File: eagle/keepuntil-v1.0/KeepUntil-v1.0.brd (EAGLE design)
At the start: 100 x 80 mm, 25 parts, among them IC1 REG1117, Q1 CSTCR6M00G53Z, T1 BC846, U1 ATMEGA328P-AU, X1 MINI-USB-32005-201

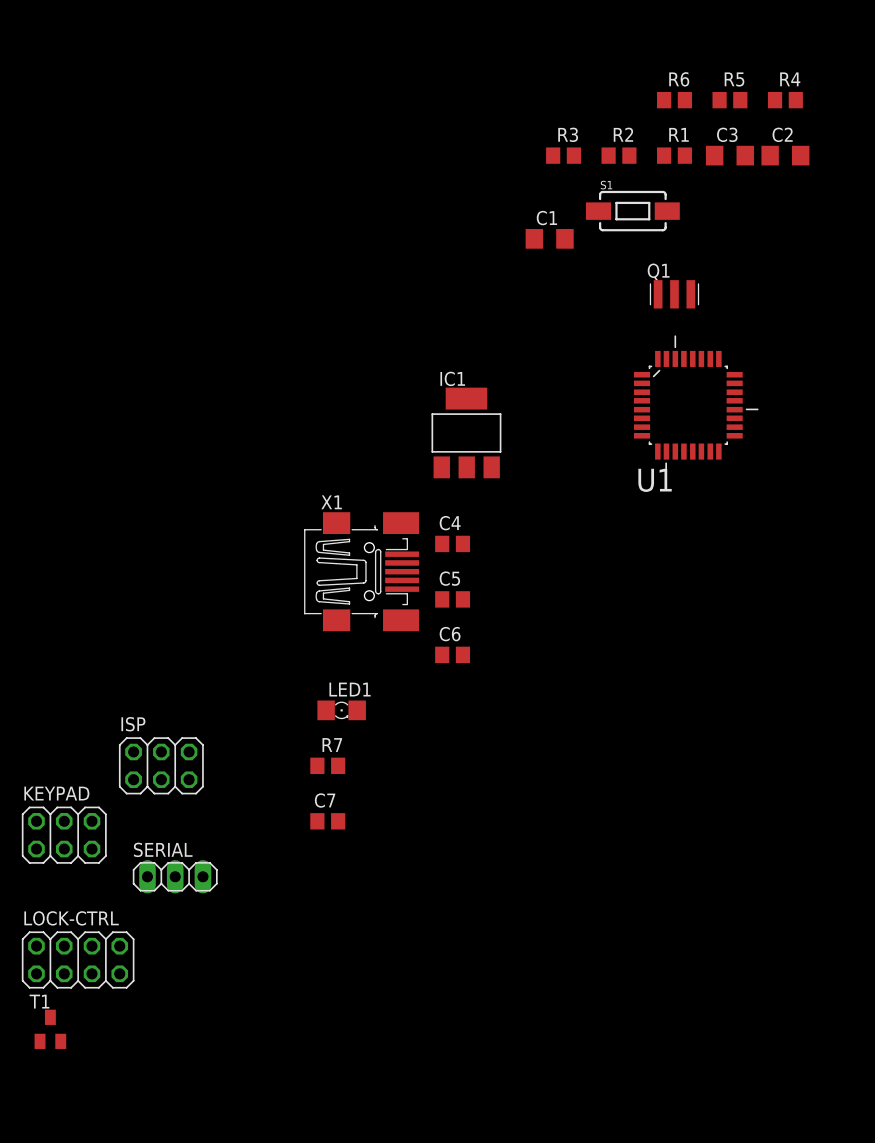
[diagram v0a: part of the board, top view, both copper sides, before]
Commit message: remove unnecessary eagle file
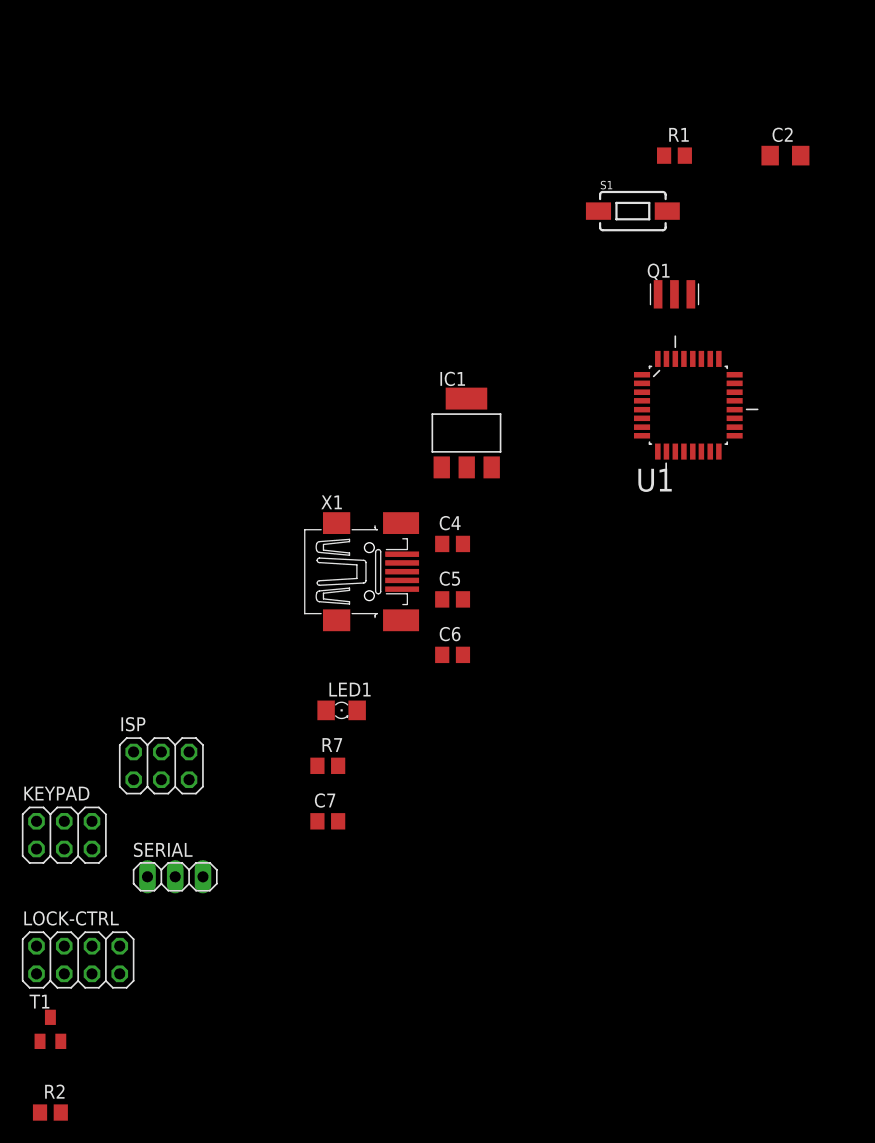
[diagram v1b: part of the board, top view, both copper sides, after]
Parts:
- removed C1, C3: (no value), resistor:C1206
- removed R3, R4, R5, R6: (no value), resistor:R0805
- moved R2 101.9 mm to (-82.5, -55.9)
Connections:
- removed net N$12: LOCK-CTRL.2
- removed net N$13: LOCK-CTRL.4
- removed net N$6: C1.2, C3.1
- new net N$3: R2.1, T1.1
- new net SOLENOID-SIG: R2.2, U1.32
- net SOLENOID: now also LOCK-CTRL.2, T1.3; no longer U1.32
- net VCC: now also LOCK-CTRL.4
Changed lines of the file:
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@@
 </autorouter>
 <elements>
-<element name="C1" library="resistor" package="C1206" value="" x="-36.83" y="24.13"/>
 <element name="C2" library="resistor" package="C1206" value="" x="-15.24" y="31.75"/>
-<element name="C3" library="resistor" package="C1206" value="" x="-20.32" y="31.75"/>
 <element name="Q1" library="murata-filter" package="CSTCR6M" value="CSTCR6M00G53Z" x="-25.4" y="19.05">
 <attribute name="MF" value="" x="-25.4" y="19.05" size="1.778" layer="27" display="off"/>
@@
 </element>
 <element name="R1" library="resistor" package="R0805" value="" x="-25.4" y="31.75"/>
-<element name="R2" library="resistor" package="R0805" value="" x="-30.48" y="31.75"/>
-<element name="R3" library="resistor" package="R0805" value="" x="-35.56" y="31.75"/>
-<element name="R4" library="resistor" package="R0805" value="" x="-15.24" y="36.83"/>
-<element name="R5" library="resistor" package="R0805" value="" x="-20.32" y="36.83"/>
-<element name="R6" library="resistor" package="R0805" value="" x="-25.4" y="36.83"/>
 <element name="S1" library="SparkFun-Electromechanical" package="TACTILE-SWITCH-1101NE" value="SWITCH-MOMENTARY-2SMD-1101NE" x="-29.21" y="26.67">
 <attribute name="PROD_ID" value="SWCH-00815" x="-29.21" y="26.67" size="1.778" layer="27" display="off"/>
@@
 <element name="LOCK-CTRL" library="pinhead" package="2X04" value="" x="-80.01" y="-41.91"/>
 <element name="T1" library="transistor" package="SOT23" value="BC846" x="-82.55" y="-48.26"/>
+<element name="R2" library="resistor" package="R0805" value="" x="-82.55" y="-55.88"/>
 </elements>
 <signals>
@@
 <contactref element="U1" pad="4"/>
 <contactref element="R1" pad="2"/>
-<contactref element="R7" pad="2"/>
 <contactref element="C7" pad="1"/>
 <contactref element="ISP" pad="2"/>
 <contactref element="LOCK-CTRL" pad="3"/>
-<wire x1="-74.93" y1="-22.86" x2="-81.28" y2="-43.18" width="0" layer="19" extent="1-1"/>
+<contactref element="R7" pad="2"/>
+<contactref element="LOCK-CTRL" pad="4"/>
+<wire x1="-81.28" y1="-40.64" x2="-81.28" y2="-43.18" width="0" layer="19" extent="1-1"/>
+<wire x1="-74.93" y1="-22.86" x2="-81.28" y2="-40.64" width="0" layer="19" extent="1-1"/>
 <wire x1="-58.1" y1="-29.21" x2="-74.93" y2="-22.86" width="0" layer="19" extent="1-1"/>
 <wire x1="-56.2" y1="-24.13" x2="-58.1" y2="-29.21" width="0" layer="19" extent="1-1"/>
@@
 <wire x1="-13.84" y1="31.75" x2="-26.06" y2="26.67" width="0" layer="19" extent="1-1"/>
 </signal>
-<signal name="N$6">
-<contactref element="C1" pad="2"/>
-<contactref element="C3" pad="1"/>
-<wire x1="-21.72" y1="31.75" x2="-35.43" y2="24.13" width="0" layer="19" extent="1-1"/>
-</signal>
 <signal name="N$7">
 <contactref element="LED1" pad="A"/>
@@
 </signal>
 <signal name="ROW3">
+<contactref element="KEYPAD" pad="5"/>
 <contactref element="U1" pad="11"/>
-<contactref element="KEYPAD" pad="5"/>
 <wire x1="-25.3238" y1="4.6482" x2="-78.74" y2="-31.75" width="0" layer="19" extent="1-1"/>
 </signal>
@@
 <wire x1="-28.3718" y1="11.684" x2="-83.82" y2="-43.18" width="0" layer="19" extent="1-1"/>
 </signal>
-<signal name="SOLENOID">
+<signal name="SOLENOID-SIG">
 <contactref element="U1" pad="32"/>
+<contactref element="R2" pad="2"/>
+<wire x1="-26.924" y1="13.1318" x2="-81.6" y2="-55.88" width="0" layer="19" extent="1-1"/>
 </signal>
 <signal name="LEDGRN">
@@
 <wire x1="-19.8882" y1="11.684" x2="-76.2" y2="-40.64" width="0" layer="19" extent="1-1"/>
 </signal>
-<signal name="N$12">
-<contactref element="LOCK-CTRL" pad="2"/>
-</signal>
-<signal name="N$13">
-<contactref element="LOCK-CTRL" pad="4"/>
-</signal>
 <signal name="N$9">
 <contactref element="LOCK-CTRL" pad="5"/>
 </signal>
+<signal name="N$3">
+<contactref element="R2" pad="1"/>
+<contactref element="T1" pad="1"/>
+<wire x1="-83.5" y1="-49.36" x2="-83.5" y2="-55.88" width="0" layer="19" extent="1-1"/>
+</signal>
+<signal name="SOLENOID">
+<contactref element="LOCK-CTRL" pad="2"/>
+<contactref element="T1" pad="3"/>
+<wire x1="-83.82" y1="-40.64" x2="-82.55" y2="-47.16" width="0" layer="19" extent="1-1"/>
+</signal>
 </signals>

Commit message: update schematic
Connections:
- net 3.3V: now also T1.2
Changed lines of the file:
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@@
 <contactref element="ISP" pad="6"/>
 <contactref element="SERIAL" pad="3"/>
+<contactref element="T1" pad="2"/>
+<wire x1="-68.58" y1="-34.29" x2="-81.6" y2="-49.36" width="0" layer="19" extent="1-1"/>
 <wire x1="-69.85" y1="-22.86" x2="-68.58" y2="-34.29" width="0" layer="19" extent="1-1"/>
 <wire x1="-56.2" y1="-29.21" x2="-68.58" y2="-34.29" width="0" layer="19" extent="1-1"/>

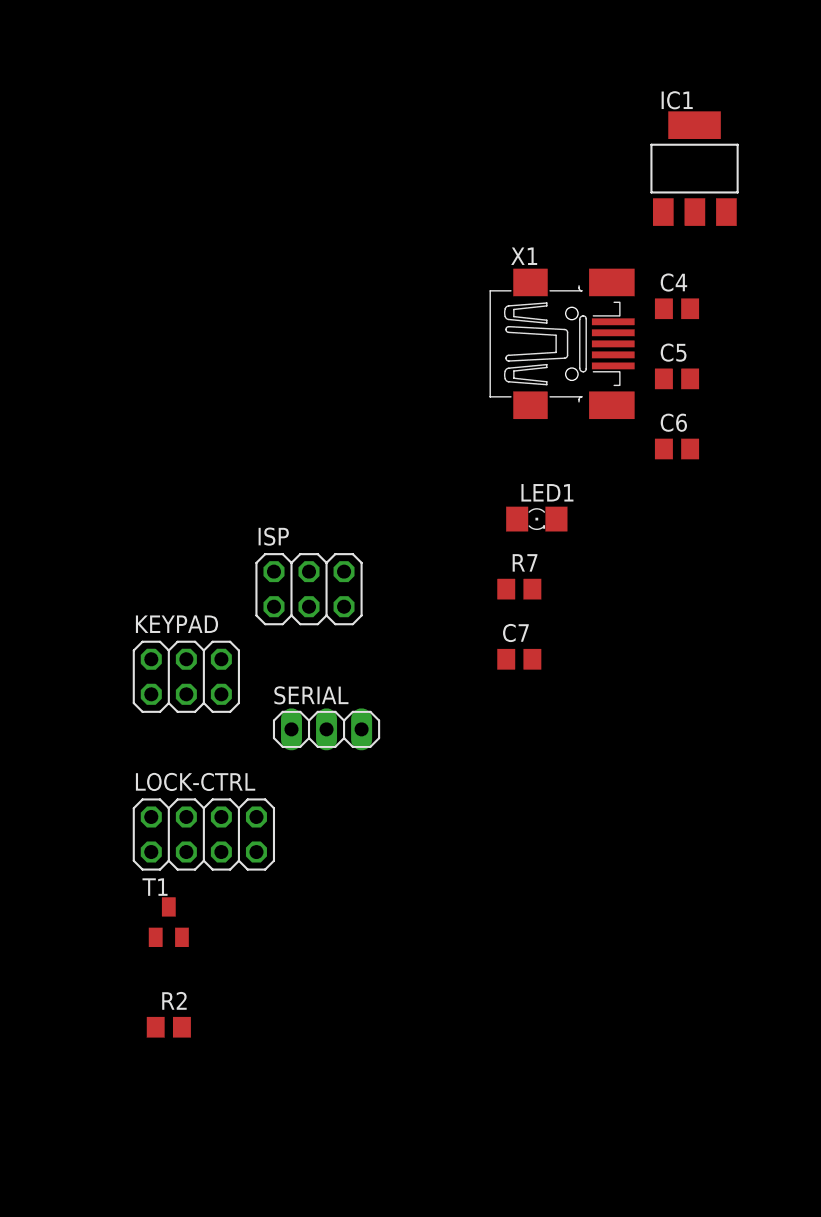
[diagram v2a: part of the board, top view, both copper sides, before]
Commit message: update schematic
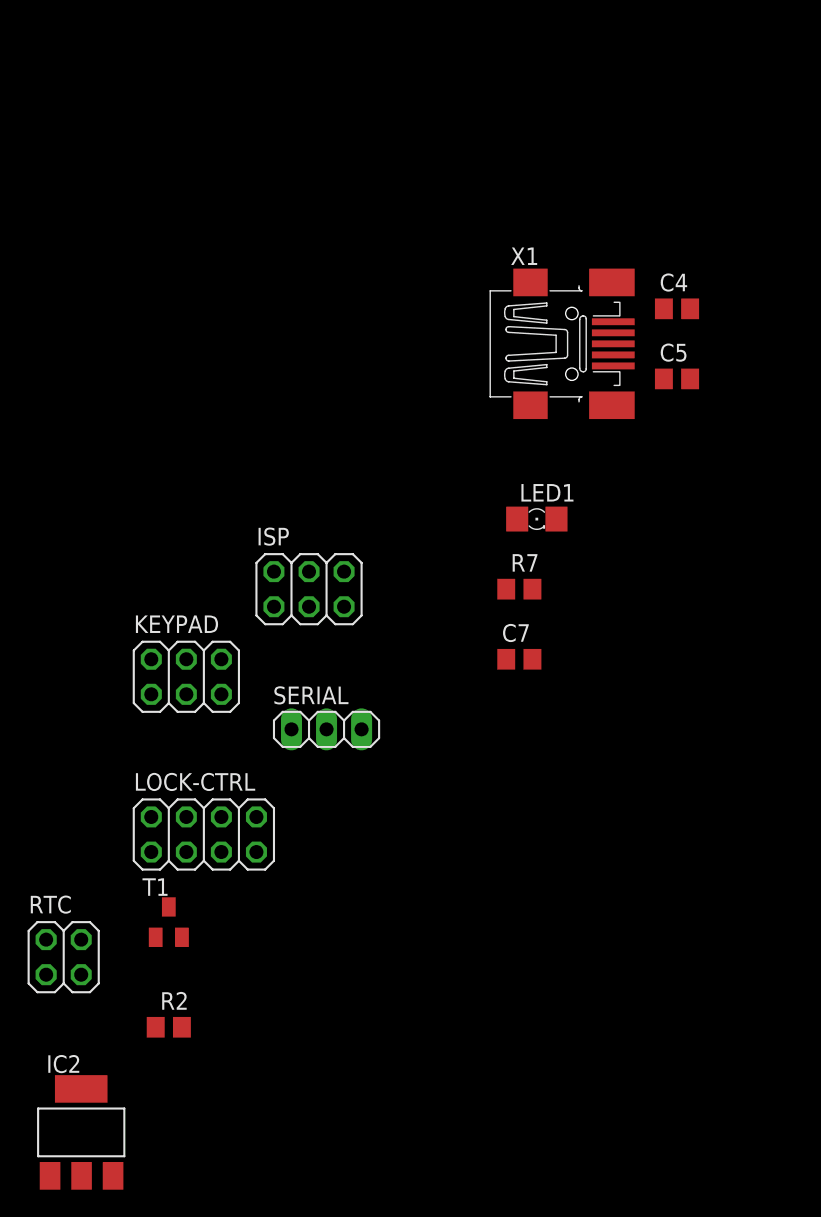
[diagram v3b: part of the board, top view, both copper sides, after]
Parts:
- removed C6: (no value), resistor:C0805
- removed IC1: REG1117, burr-brown:SOT223
- added IC2: REG1117, burr-brown:SOT223
- added RTC: (no value), pinhead:2X02
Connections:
- net LEDGRN renamed LED-GRN
- net LEDRED renamed LED-RED
- removed net 3.3V: C2.2, C4.2, C5.2, C7.2, IC1.1, ISP.6, LED1.C, S1.2, SERIAL.3, T1.2, X1.5
- removed net N$5: C4.1, IC1.3, X1.1
- removed net N$9: LOCK-CTRL.5
- removed net SCL: U1.28
- new net GND: C2.2, C4.2, C5.2, C7.2, IC2.1, ISP.6, LED1.C, LOCK-CTRL.5, RTC.4, S1.2, SERIAL.3, T1.2, U1.21, U1.3, U1.5, X1.5
- new net RTC-SCL: RTC.3, U1.28
- new net RTC-SDA: RTC.1, U1.27
- net N$4: now also C4.1, IC2.3, X1.1; no longer U1.21, U1.3, U1.5
- net VCC: now also IC2.2, RTC.2; no longer IC1.2

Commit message: schematic cleanup
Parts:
- removed C7: (no value), resistor:C0805
- removed SERIAL: (no value), pinhead:1X03
- added JP1: (no value), adafruit:1X03
- C2: value (none) -> 10uf
- C4, C5: value (none) -> 0.1uF
- R1: value (none) -> 1K
- R2: value (none) -> 10K
- R7: value (none) -> 330
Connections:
- net GND: now also JP1.3; no longer C7.2, SERIAL.3
- net RX: now also JP1.1; no longer SERIAL.1
- net TX: now also JP1.2; no longer SERIAL.2
- net VCC: no longer C7.1
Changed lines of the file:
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@@
 <setting verticaltext="up"/>
 </settings>
-<grid distance="0.05" unitdist="inch" unit="inch" style="lines" multiple="1" display="no" altdistance="0.025" altunitdist="inch" altunit="inch"/>
+<grid distance="0.5" unitdist="mm" unit="mm" style="lines" multiple="1" display="no" altdistance="0.1" altunitdist="mm" altunit="mm"/>
 <layers>
 <layer number="1" name="Top" color="4" fill="1" visible="yes" active="yes"/>
@@
 <layer number="43" name="vRestrict" color="2" fill="10" visible="yes" active="yes"/>
 <layer number="44" name="Drills" color="7" fill="1" visible="no" active="yes"/>
-<layer number="45" name="Holes" color="7" fill="1" visible="no" active="yes"/>
+<layer number="45" name="Holes" color="7" fill="1" visible="yes" active="yes"/>
 <layer number="46" name="Milling" color="3" fill="1" visible="no" active="yes"/>
 <layer number="47" name="Measures" color="7" fill="1" visible="no" active="yes"/>
@@
 </autorouter>
 <elements>
-<element name="C2" library="resistor" package="C1206" value="" x="-15.24" y="31.75"/>
+<element name="C2" library="resistor" package="C1206" value="10uf" x="-15.24" y="31.75"/>
 <element name="Q1" library="murata-filter" package="CSTCR6M" value="CSTCR6M00G53Z" x="-25.4" y="19.05">
 <attribute name="MF" value="" x="-25.4" y="19.05" size="1.778" layer="27" display="off"/>
@@
 <attribute name="OC_NEWARK" value="25M8759" x="-25.4" y="19.05" size="1.778" layer="27" display="off"/>
 </element>
-<element name="R1" library="resistor" package="R0805" value="" x="-25.4" y="31.75"/>
+<element name="R1" library="resistor" package="R0805" value="1K" x="-25.4" y="31.75"/>
 <element name="S1" library="SparkFun-Electromechanical" package="TACTILE-SWITCH-1101NE" value="SWITCH-MOMENTARY-2SMD-1101NE" x="-29.21" y="26.67">
 <attribute name="PROD_ID" value="SWCH-00815" x="-29.21" y="26.67" size="1.778" layer="27" display="off"/>
@@
 <attribute name="OC_NEWARK" value="14R4631" x="-24.13" y="8.89" size="1.778" layer="27" display="off"/>
 </element>
-<element name="C4" library="resistor" package="C0805" value="" x="-45.72" y="-3.81"/>
-<element name="C5" library="resistor" package="C0805" value="" x="-45.72" y="-8.89"/>
+<element name="C4" library="resistor" package="C0805" value="0.1uF" x="-45.72" y="-3.81"/>
+<element name="C5" library="resistor" package="C0805" value="0.1uF" x="-45.72" y="-8.89"/>
 <element name="X1" library="con-cypressindustries" package="32005-201" value="MINI-USB-32005-201" x="-53.34" y="-6.35">
 <attribute name="OC_FARNELL" value="unknown" x="-53.34" y="-6.35" size="1.778" layer="27" display="off"/>
@@
 </element>
 <element name="LED1" library="led" package="1206" value="" x="-55.88" y="-19.05"/>
-<element name="R7" library="resistor" package="R0805" value="" x="-57.15" y="-24.13"/>
-<element name="C7" library="resistor" package="C0805" value="" x="-57.15" y="-29.21"/>
+<element name="R7" library="resistor" package="R0805" value="330" x="-57.15" y="-24.13"/>
 <element name="ISP" library="pinhead" package="2X03" value="" x="-72.39" y="-24.13"/>
-<element name="SERIAL" library="pinhead" package="1X03" value="" x="-71.12" y="-34.29"/>
 <element name="KEYPAD" library="pinhead" package="2X03" value="" x="-81.28" y="-30.48"/>
 <element name="LOCK-CTRL" library="pinhead" package="2X04" value="" x="-80.01" y="-41.91"/>
 <element name="T1" library="transistor" package="SOT23" value="BC846" x="-82.55" y="-48.26"/>
-<element name="R2" library="resistor" package="R0805" value="" x="-82.55" y="-55.88"/>
+<element name="R2" library="resistor" package="R0805" value="10K" x="-82.55" y="-55.88"/>
 <element name="RTC" library="pinhead" package="2X02" value="" x="-90.17" y="-50.8"/>
 <element name="IC2" library="burr-brown" package="SOT223" value="REG1117" x="-88.9" y="-63.5">
@@
 <attribute name="MF" value="" x="-97.79" y="-49.53" size="1.778" layer="27" display="off"/>
 </element>
+<element name="JP1" library="adafruit" package="1X03" value="" x="-87.63" y="-73.66"/>
 </elements>
 <signals>
@@
 <signal name="TX">
 <contactref element="U1" pad="31"/>
-<contactref element="SERIAL" pad="2"/>
-<wire x1="-26.1366" y1="13.1318" x2="-71.12" y2="-34.29" width="0" layer="19" extent="1-1"/>
+<contactref element="JP1" pad="2"/>
+<wire x1="-26.1366" y1="13.1318" x2="-87.63" y2="-73.66" width="0" layer="19" extent="1-1"/>
 </signal>
 <signal name="RX">
 <contactref element="U1" pad="30"/>
-<contactref element="SERIAL" pad="1"/>
-<wire x1="-25.3238" y1="13.1318" x2="-73.66" y2="-34.29" width="0" layer="19" extent="1-1"/>
+<contactref element="JP1" pad="1"/>
+<wire x1="-25.3238" y1="13.1318" x2="-90.17" y2="-73.66" width="0" layer="19" extent="1-1"/>
 </signal>
 <signal name="ROW1">
@@
 <contactref element="IC2" pad="2"/>
 <contactref element="C2" pad="1"/>
-<contactref element="C7" pad="1"/>
 <contactref element="R7" pad="2"/>
 <wire x1="-91.44" y1="-49.53" x2="-88.8746" y2="-66.6496" width="0" layer="19" extent="1-1"/>
@@
 <wire x1="-81.28" y1="-40.64" x2="-81.28" y2="-43.18" width="0" layer="19" extent="1-1"/>
 <wire x1="-74.93" y1="-22.86" x2="-81.28" y2="-40.64" width="0" layer="19" extent="1-1"/>
-<wire x1="-58.1" y1="-29.21" x2="-74.93" y2="-22.86" width="0" layer="19" extent="1-1"/>
-<wire x1="-56.2" y1="-24.13" x2="-58.1" y2="-29.21" width="0" layer="19" extent="1-1"/>
+<wire x1="-56.2" y1="-24.13" x2="-74.93" y2="-22.86" width="0" layer="19" extent="1-1"/>
 <wire x1="-28.3718" y1="7.6962" x2="-56.2" y2="-24.13" width="0" layer="19" extent="1-1"/>
 <wire x1="-28.3718" y1="9.2964" x2="-28.3718" y2="7.6962" width="0" layer="19" extent="1-1"/>
@@
 <contactref element="C4" pad="2"/>
 <contactref element="C2" pad="2"/>
-<contactref element="C7" pad="2"/>
 <contactref element="LED1" pad="C"/>
 <contactref element="S1" pad="2"/>
@@
 <contactref element="T1" pad="2"/>
 <contactref element="ISP" pad="6"/>
-<contactref element="SERIAL" pad="3"/>
 <contactref element="RTC" pad="4"/>
 <contactref element="X1" pad="5"/>
 <contactref element="LOCK-CTRL" pad="5"/>
 <contactref element="IC2" pad="1"/>
+<contactref element="JP1" pad="3"/>
+<wire x1="-91.1606" y1="-66.6496" x2="-85.09" y2="-73.66" width="0" layer="19" extent="1-1"/>
 <wire x1="-88.9" y1="-49.53" x2="-91.1606" y2="-66.6496" width="0" layer="19" extent="1-1"/>
 <wire x1="-81.6" y1="-49.36" x2="-88.9" y2="-49.53" width="0" layer="19" extent="1-1"/>
 <wire x1="-78.74" y1="-43.18" x2="-81.6" y2="-49.36" width="0" layer="19" extent="1-1"/>
-<wire x1="-68.58" y1="-34.29" x2="-78.74" y2="-43.18" width="0" layer="19" extent="1-1"/>
-<wire x1="-69.85" y1="-22.86" x2="-68.58" y2="-34.29" width="0" layer="19" extent="1-1"/>
-<wire x1="-56.2" y1="-29.21" x2="-68.58" y2="-34.29" width="0" layer="19" extent="1-1"/>
-<wire x1="-54.458" y1="-19.05" x2="-56.2" y2="-29.21" width="0" layer="19" extent="1-1"/>
+<wire x1="-69.85" y1="-22.86" x2="-78.74" y2="-43.18" width="0" layer="19" extent="1-1"/>
+<wire x1="-54.458" y1="-19.05" x2="-69.85" y2="-22.86" width="0" layer="19" extent="1-1"/>
 <wire x1="-50.34" y1="-7.95" x2="-54.458" y2="-19.05" width="0" layer="19" extent="1-1"/>
 <wire x1="-44.77" y1="-8.89" x2="-50.34" y2="-7.95" width="0" layer="19" extent="1-1"/>
